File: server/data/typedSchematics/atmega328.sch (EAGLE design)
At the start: 7 parts, among them U3 ATMEGA328, Y1 8MHz

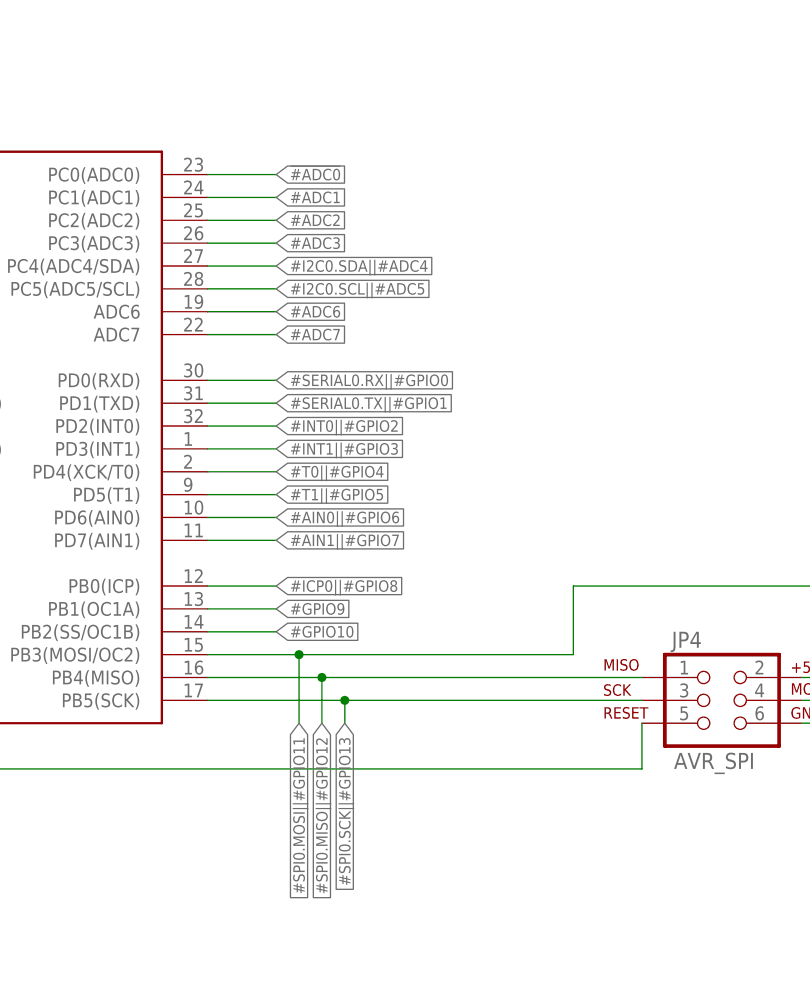
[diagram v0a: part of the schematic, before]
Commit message: Redefining typed annotation
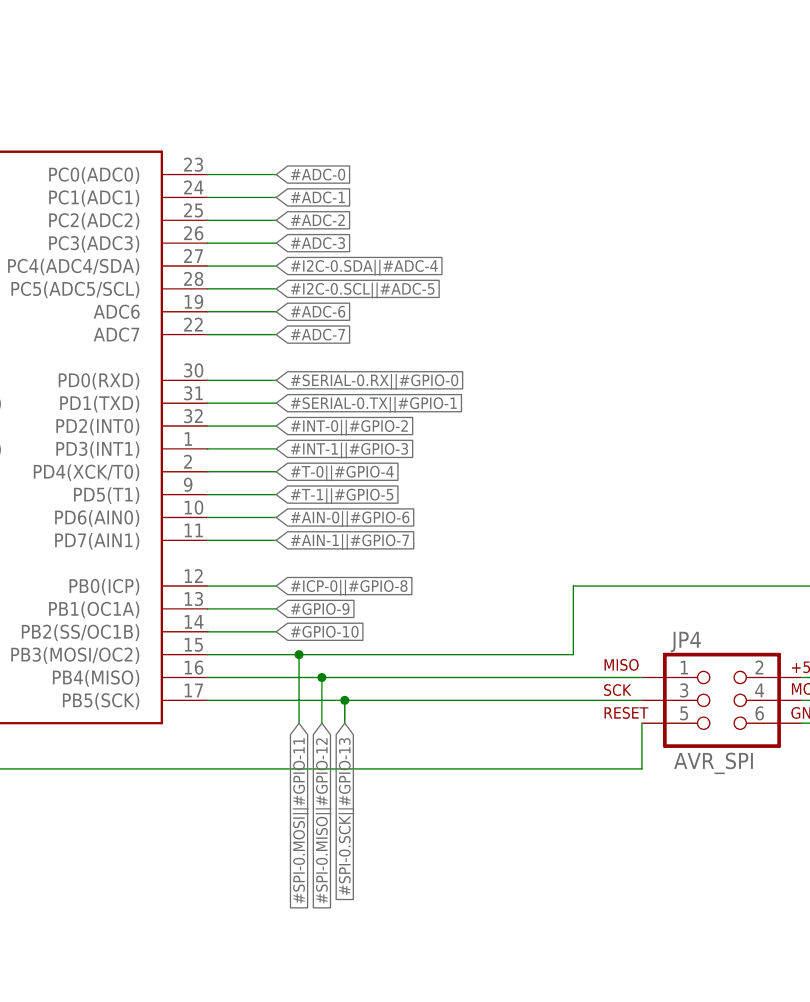
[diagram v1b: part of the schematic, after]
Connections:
- net !#ADC0 renamed #ADC-0
- net #ADC1 renamed #ADC-1
- net #ADC2 renamed #ADC-2
- net #ADC3 renamed #ADC-3
- net #ADC6 renamed #ADC-6
- net #ADC7 renamed #ADC-7
- net #AIN0||#GPIO6 renamed #AIN-0||#GPIO-6
- net #AIN1||#GPIO7 renamed #AIN-1||#GPIO-7
- net #GPIO10 renamed #GPIO-10
- net #GPIO9 renamed #GPIO-9
- net #I2C0.SCL||#ADC5 renamed #I2C-0.SCL||#ADC-5
- net #I2C0.SDA||#ADC4 renamed #I2C-0.SDA||#ADC-4
- net #ICP0||#GPIO8 renamed #ICP-0||#GPIO-8
- net #INT0||#GPIO2 renamed #INT-0||#GPIO-2
- net #INT1||#GPIO3 renamed #INT-1||#GPIO-3
- net #SERIAL0.RX||#GPIO0 renamed #SERIAL-0.RX||#GPIO-0
- net #SERIAL0.TX||#GPIO1 renamed #SERIAL-0.TX||#GPIO-1
- net #SPI0.MISO||#GPIO12 renamed #SPI-0.MISO||#GPIO-12
- net #SPI0.MOSI||#GPIO11 renamed #SPI-0.MOSI||#GPIO-11
- net #SPI0.SCK||#GPIO13 renamed #SPI-0.SCK||#GPIO-13
- net #T0||#GPIO4 renamed #T-0||#GPIO-4
- net #T1||#GPIO5 renamed #T-1||#GPIO-5
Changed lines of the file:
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@@
 </segment>
 </net>
-<net name="!#ADC0" class="0">
+<net name="#ADC-0" class="0">
 <segment>
 <pinref part="U3" gate="G$1" pin="PC0(ADC0)"/>
@@
 </segment>
 </net>
-<net name="#ADC1" class="0">
+<net name="#ADC-1" class="0">
 <segment>
 <pinref part="U3" gate="G$1" pin="PC1(ADC1)"/>
@@
 </segment>
 </net>
-<net name="#ADC2" class="0">
+<net name="#ADC-2" class="0">
 <segment>
 <pinref part="U3" gate="G$1" pin="PC2(ADC2)"/>
@@
 </segment>
 </net>
-<net name="#ADC3" class="0">
+<net name="#ADC-3" class="0">
 <segment>
 <pinref part="U3" gate="G$1" pin="PC3(ADC3)"/>
@@
 </segment>
 </net>
-<net name="#I2C0.SDA||#ADC4" class="0">
+<net name="#I2C-0.SDA||#ADC-4" class="0">
 <segment>
 <pinref part="U3" gate="G$1" pin="PC4(ADC4/SDA)"/>
@@
 </segment>
 </net>
-<net name="#I2C0.SCL||#ADC5" class="0">
+<net name="#I2C-0.SCL||#ADC-5" class="0">
 <segment>
 <pinref part="U3" gate="G$1" pin="PC5(ADC5/SCL)"/>
@@
 </segment>
 </net>
-<net name="#ADC6" class="0">
+<net name="#ADC-6" class="0">
 <segment>
 <pinref part="U3" gate="G$1" pin="ADC6"/>
@@
 </segment>
 </net>
-<net name="#ADC7" class="0">
+<net name="#ADC-7" class="0">
 <segment>
 <pinref part="U3" gate="G$1" pin="ADC7"/>
@@
 </segment>
 </net>
-<net name="#SPI0.MOSI||#GPIO11" class="0">
+<net name="#SPI-0.MOSI||#GPIO-11" class="0">
 <segment>
 <pinref part="JP4" gate="G$1" pin="4"/>
@@
 </segment>
 </net>
-<net name="#SPI0.MISO||#GPIO12" class="0">
+<net name="#SPI-0.MISO||#GPIO-12" class="0">
 <segment>
 <pinref part="U3" gate="G$1" pin="PB4(MISO)"/>
@@
 </segment>
 </net>
-<net name="#SPI0.SCK||#GPIO13" class="0">
+<net name="#SPI-0.SCK||#GPIO-13" class="0">
 <segment>
 <pinref part="JP4" gate="G$1" pin="3"/>
@@
 </segment>
 </net>
-<net name="#SERIAL0.RX||#GPIO0" class="0">
+<net name="#SERIAL-0.RX||#GPIO-0" class="0">
 <segment>
 <pinref part="U3" gate="G$1" pin="PD0(RXD)"/>
@@
 </segment>
 </net>
-<net name="#SERIAL0.TX||#GPIO1" class="0">
+<net name="#SERIAL-0.TX||#GPIO-1" class="0">
 <segment>
 <pinref part="U3" gate="G$1" pin="PD1(TXD)"/>
@@
 </segment>
 </net>
-<net name="#INT0||#GPIO2" class="0">
+<net name="#INT-0||#GPIO-2" class="0">
 <segment>
 <pinref part="U3" gate="G$1" pin="PD2(INT0)"/>
@@
 </segment>
 </net>
-<net name="#INT1||#GPIO3" class="0">
+<net name="#INT-1||#GPIO-3" class="0">
 <segment>
 <pinref part="U3" gate="G$1" pin="PD3(INT1)"/>
@@
 </segment>
 </net>
-<net name="#T0||#GPIO4" class="0">
+<net name="#T-0||#GPIO-4" class="0">
 <segment>
 <pinref part="U3" gate="G$1" pin="PD4(XCK/T0)"/>
@@
 </segment>
 </net>
-<net name="#T1||#GPIO5" class="0">
+<net name="#T-1||#GPIO-5" class="0">
 <segment>
 <pinref part="U3" gate="G$1" pin="PD5(T1)"/>
@@
 </segment>
 </net>
-<net name="#AIN0||#GPIO6" class="0">
+<net name="#AIN-0||#GPIO-6" class="0">
 <segment>
 <pinref part="U3" gate="G$1" pin="PD6(AIN0)"/>
@@
 </segment>
 </net>
-<net name="#AIN1||#GPIO7" class="0">
+<net name="#AIN-1||#GPIO-7" class="0">
 <segment>
 <pinref part="U3" gate="G$1" pin="PD7(AIN1)"/>
@@
 </segment>
 </net>
-<net name="#ICP0||#GPIO8" class="0">
+<net name="#ICP-0||#GPIO-8" class="0">
 <segment>
 <pinref part="U3" gate="G$1" pin="PB0(ICP)"/>
@@
 </segment>
 </net>
-<net name="#GPIO9" class="0">
+<net name="#GPIO-9" class="0">
 <segment>
 <pinref part="U3" gate="G$1" pin="PB1(OC1A)"/>
@@
 </segment>
 </net>
-<net name="#GPIO10" class="0">
+<net name="#GPIO-10" class="0">
 <segment>
 <pinref part="U3" gate="G$1" pin="PB2(SS/OC1B)"/>

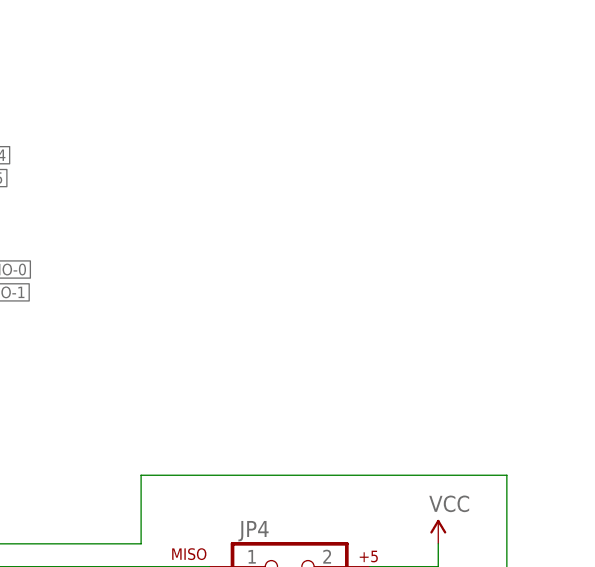
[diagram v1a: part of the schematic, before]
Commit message: Adding example for text annotations
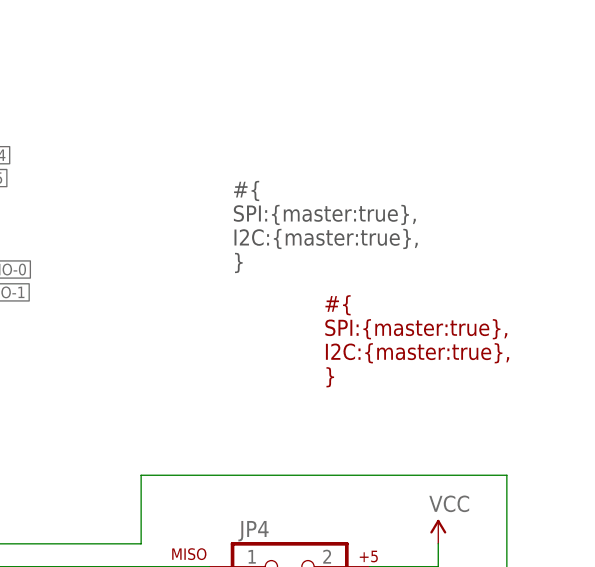
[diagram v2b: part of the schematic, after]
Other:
- note added: "#{ SPI:{master:true}, I2C:{master:true}, }"
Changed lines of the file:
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@@
 <sheet>
 <plain>
+<text x="175.26" y="101.6" size="1.778" layer="97">#{
+SPI:{master:true},
+I2C:{master:true},
+}</text>
+<text x="185.42" y="88.9" size="1.778" layer="94">#{
+SPI:{master:true},
+I2C:{master:true},
+}</text>
 </plain>
 <instances>
@@
 </drawing>
 <compatibility>
+<note version="6.3" minversion="6.2.2" severity="warning">
+Since Version 6.2.2 text objects can contain more than one line,
+which will not be processed correctly with this version.
+</note>
 <note version="8.2" severity="warning">
 Since Version 8.2, EAGLE supports online libraries. The ids

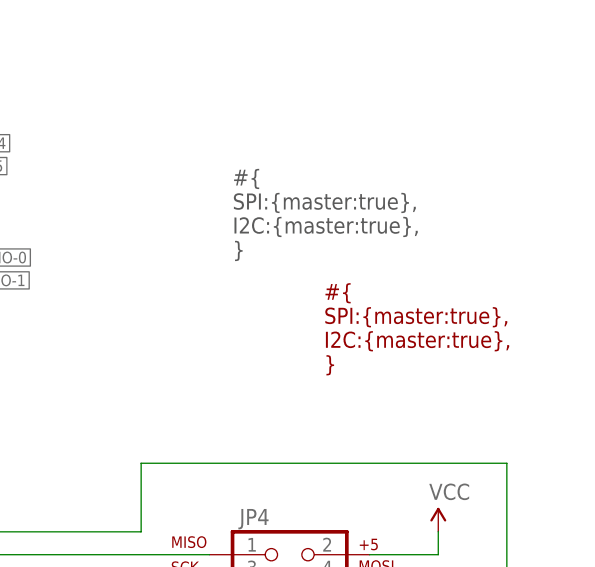
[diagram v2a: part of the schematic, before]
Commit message: Adding master-slave constrain to SPI
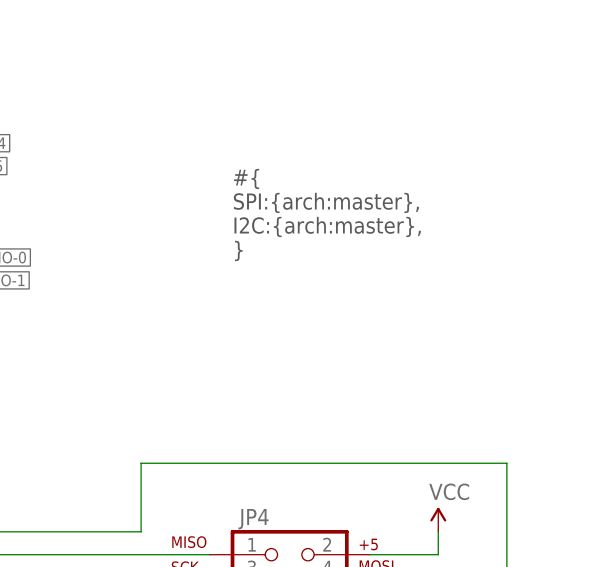
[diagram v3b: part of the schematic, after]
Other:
- note added: "#{ SPI:{arch:master}, I2C:{arch:master}, }"
- note removed: "#{ SPI:{master:true}, I2C:{master:true}, }"
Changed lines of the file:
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@@
 <plain>
 <text x="175.26" y="101.6" size="1.778" layer="97">#{
-SPI:{master:true},
-I2C:{master:true},
-}</text>
-<text x="185.42" y="88.9" size="1.778" layer="94">#{
-SPI:{master:true},
-I2C:{master:true},
+SPI:{arch:master},
+I2C:{arch:master},
 }</text>
 </plain>

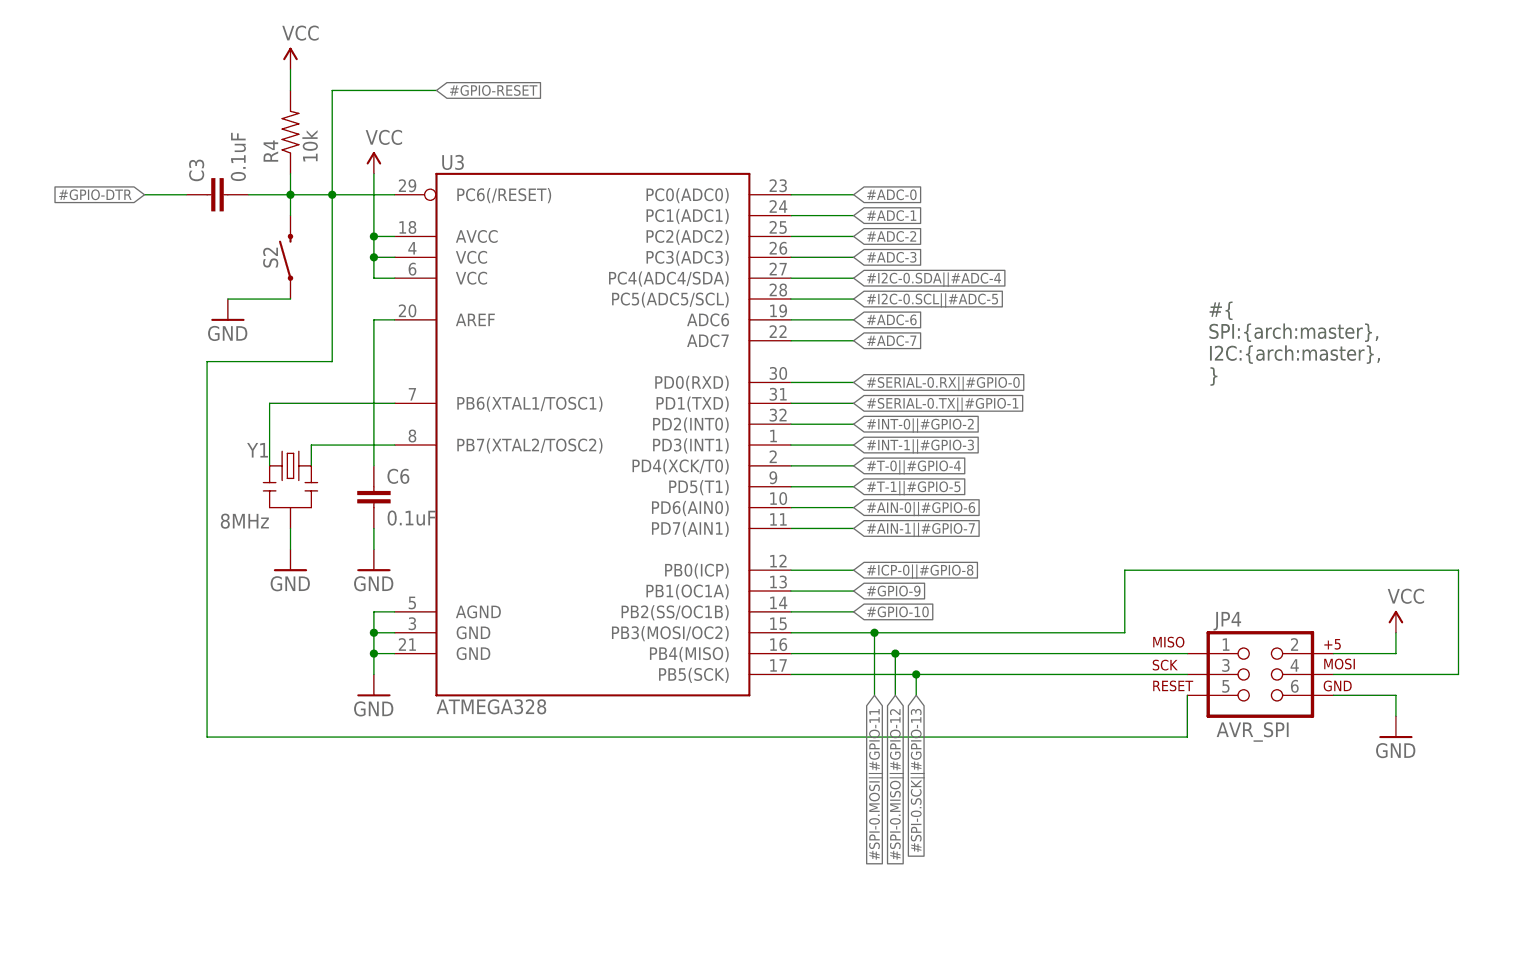
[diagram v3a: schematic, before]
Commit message: Add typed power
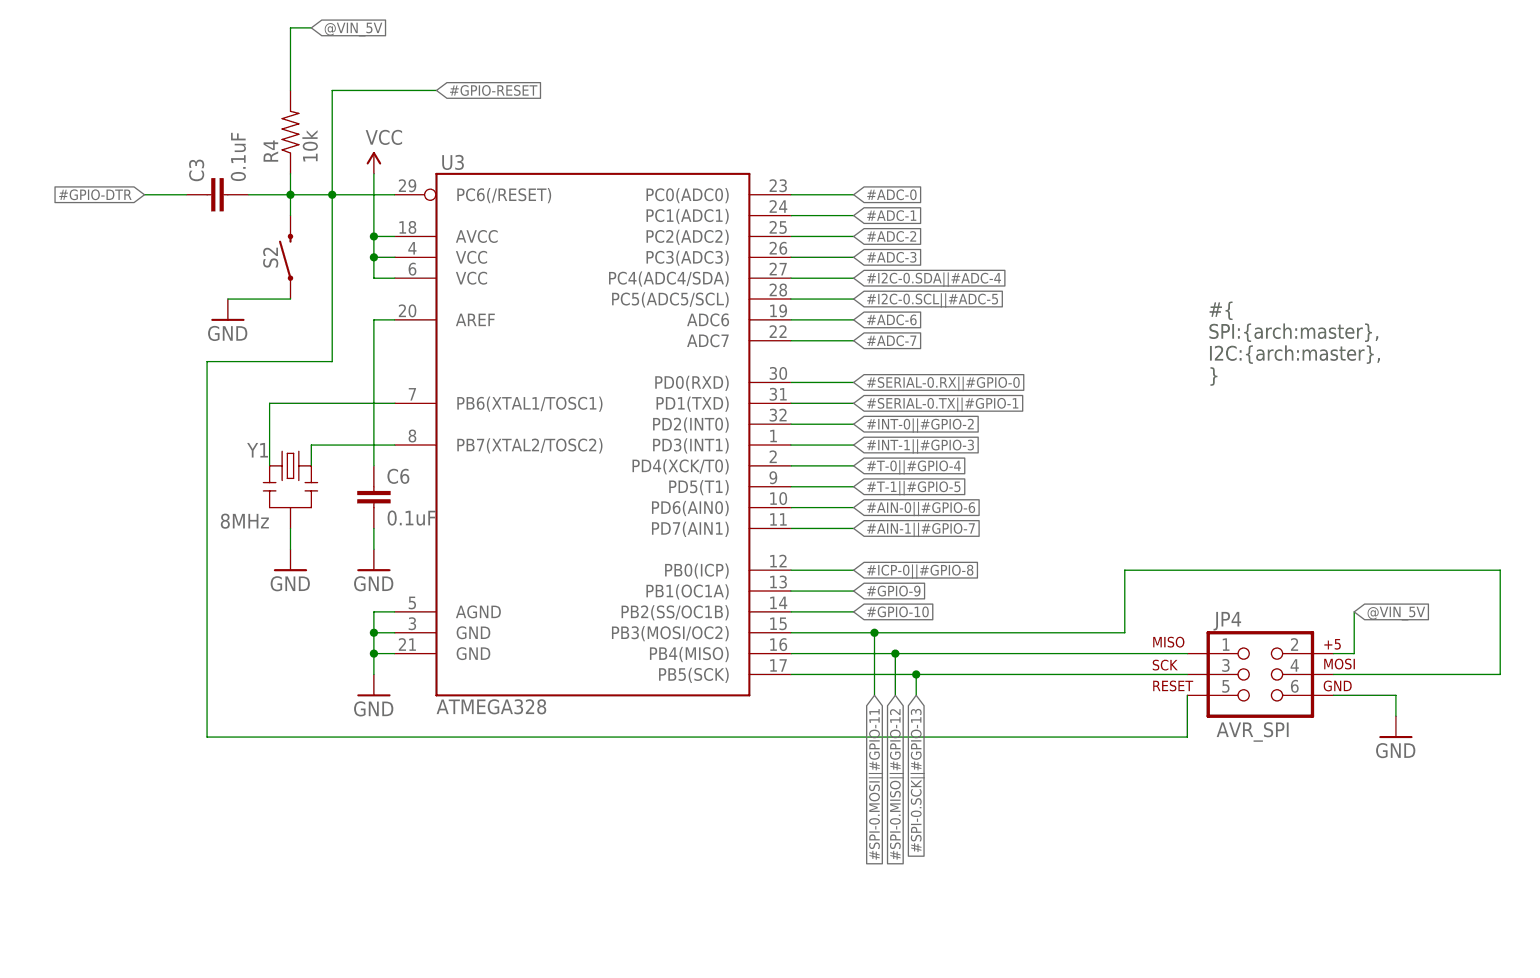
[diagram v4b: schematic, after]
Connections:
- new net @VIN_5V: JP4.2, R4.2
- net VCC: no longer JP4.2, R4.2
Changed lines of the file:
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@@
 <part name="U3" library="SparkFun" deviceset="ATMEGA168" device="" value="ATMEGA328"/>
 <part name="GND5" library="SparkFun" deviceset="GND" device=""/>
-<part name="P+2" library="SparkFun" deviceset="VCC" device=""/>
 <part name="GND6" library="SparkFun" deviceset="GND" device=""/>
 <part name="P+3" library="SparkFun" deviceset="VCC" device=""/>
 <part name="JP4" library="SparkFun" deviceset="AVR_SPI_PRG_6" device="PTH" value="AVR_SPI"/>
-<part name="P+1" library="SparkFun" deviceset="VCC" device=""/>
 <part name="GND1" library="SparkFun" deviceset="GND" device=""/>
 <part name="R4" library="SparkFun-Resistors" library_urn="urn:adsk.eagle:library:532" deviceset="10KOHM" device="-0603-1/10W-1%" package3d_urn="urn:adsk.eagle:package:39650/1" value="10k"/>
@@
 <attribute name="VALUE" x="71.12" y="60.96" size="1.778" layer="96"/>
 </instance>
-<instance part="P+2" gate="1" x="63.5" y="139.7" smashed="yes">
-<attribute name="VALUE" x="62.484" y="143.256" size="1.778" layer="96"/>
-</instance>
 <instance part="GND6" gate="1" x="55.88" y="109.22" smashed="yes">
 <attribute name="VALUE" x="53.34" y="106.68" size="1.778" layer="96"/>
@@
 <attribute name="NAME" x="176.022" y="71.882" size="1.778" layer="95"/>
 <attribute name="VALUE" x="176.276" y="58.42" size="1.778" layer="96"/>
-</instance>
-<instance part="P+1" gate="1" x="198.12" y="71.12" smashed="yes">
-<attribute name="VALUE" x="197.104" y="74.676" size="1.778" layer="96"/>
 </instance>
 <instance part="GND1" gate="1" x="198.12" y="58.42" smashed="yes">
@@
 <net name="VCC" class="1">
 <segment>
-<wire x1="63.5" y1="137.16" x2="63.5" y2="139.7" width="0.1524" layer="91"/>
-<pinref part="P+2" gate="1" pin="VCC"/>
-<pinref part="R4" gate="G$1" pin="2"/>
-</segment>
-<segment>
 <wire x1="76.2" y1="114.3" x2="73.66" y2="114.3" width="0.1524" layer="91"/>
 <wire x1="73.66" y1="114.3" x2="73.66" y2="116.84" width="0.1524" layer="91"/>
@@
 <pinref part="U3" gate="G$1" pin="VCC@2"/>
 <pinref part="U3" gate="G$1" pin="AVCC"/>
-</segment>
-<segment>
-<wire x1="190.5" y1="68.58" x2="198.12" y2="68.58" width="0.1524" layer="91"/>
-<wire x1="198.12" y1="71.12" x2="198.12" y2="68.58" width="0.1524" layer="91"/>
-<pinref part="JP4" gate="G$1" pin="2"/>
-<pinref part="P+1" gate="1" pin="VCC"/>
 </segment>
 </net>
@@
 <segment>
 <pinref part="JP4" gate="G$1" pin="4"/>
-<wire x1="190.5" y1="66.04" x2="205.74" y2="66.04" width="0.1524" layer="91"/>
-<wire x1="205.74" y1="66.04" x2="205.74" y2="78.74" width="0.1524" layer="91"/>
-<wire x1="205.74" y1="78.74" x2="165.1" y2="78.74" width="0.1524" layer="91"/>
+<wire x1="190.5" y1="66.04" x2="210.82" y2="66.04" width="0.1524" layer="91"/>
+<wire x1="210.82" y1="66.04" x2="210.82" y2="78.74" width="0.1524" layer="91"/>
+<wire x1="210.82" y1="78.74" x2="165.1" y2="78.74" width="0.1524" layer="91"/>
 <pinref part="U3" gate="G$1" pin="PB3(MOSI/OC2)"/>
 <wire x1="165.1" y1="78.74" x2="165.1" y2="71.12" width="0.1524" layer="91"/>
@@
 </segment>
 </net>
+<net name="@VIN_5V" class="0">
+<segment>
+<pinref part="R4" gate="G$1" pin="2"/>
+<wire x1="63.5" y1="137.16" x2="63.5" y2="144.78" width="0.1524" layer="91"/>
+<wire x1="63.5" y1="144.78" x2="66.04" y2="144.78" width="0.1524" layer="91"/>
+<label x="66.04" y="144.78" size="1.27" layer="95" xref="yes"/>
+</segment>
+<segment>
+<pinref part="JP4" gate="G$1" pin="2"/>
+<wire x1="190.5" y1="68.58" x2="193.04" y2="68.58" width="0.1524" layer="91"/>
+<wire x1="193.04" y1="68.58" x2="193.04" y2="73.66" width="0.1524" layer="91"/>
+<label x="193.04" y="73.66" size="1.27" layer="95" xref="yes"/>
+</segment>
+</net>
